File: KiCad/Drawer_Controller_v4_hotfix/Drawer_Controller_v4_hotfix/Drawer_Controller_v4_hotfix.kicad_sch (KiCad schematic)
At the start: 21 parts, among them J1 Conn_02x05_Odd_Even, J2 Conn_02x03_Odd_Even, J3 Conn_02x04_Odd_Even, U1 PESD2CANFD24L-TR, X1 RJ45_45_degree_angled, X2 Conn_01x02_2.5mm_JST_S02B-XAS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, X3 Conn_01x08_2.5mm_JST_S04B-XAS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, X4 Conn_02x03_3.0mm_Molex_Micro_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, X5 Conn_01x03_2.5mm_JST_S04B-XAS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, X6 Conn_01x04_2.5mm_JST_S04B-XAS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

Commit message: fix: adds `in_bom` attribute for two parts
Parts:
- X1, X4: now in the parts list
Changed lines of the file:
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@@
 		(unit 1)
 		(exclude_from_sim no)
-		(in_bom no)
+		(in_bom yes)
 		(on_board yes)
 		(dnp no)
@@
 		(unit 1)
 		(exclude_from_sim no)
-		(in_bom no)
-		(on_board yes)
-		(dnp no)
+		(in_bom yes)
+		(on_board yes)
+		(dnp no)

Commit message: feat: adds `durability` attribute to `Drawer_Controller_v4_hotfix`
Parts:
- C1: durability (none) -> 5000h@105°C
- X1: durability (none) -> 500 Mating cycles
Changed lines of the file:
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@@
 			)
 		)
+		(property "durability" ""
+			(at 340.36 80.01 0)
+			(effects
+				(font
+					(size 1.27 1.27)
+				)
+				(hide yes)
+			)
+		)
 		(pin "3"
 		)
@@
 			)
 		)
+		(property "durability" ""
+			(at 255.27 133.35 0)
+			(effects
+				(font
+					(size 1.27 1.27)
+				)
+				(hide yes)
+			)
+		)
 		(instances
 			(project "Drawer_Controller_v4"
@@
 			)
 		)
+		(property "durability" ""
+			(at 287.02 34.29 0)
+			(effects
+				(font
+					(size 1.27 1.27)
+				)
+				(hide yes)
+			)
+		)
 		(pin "6"
 		)
@@
 			)
 		)
+		(property "durability" ""
+			(at 97.79 121.92 0)
+			(effects
+				(font
+					(size 1.27 1.27)
+				)
+				(hide yes)
+			)
+		)
 		(pin "2"
 		)
@@
 			)
 		)
+		(property "durability" ""
+			(at 255.27 138.43 0)
+			(effects
+				(font
+					(size 1.27 1.27)
+				)
+				(hide yes)
+			)
+		)
 		(instances
 			(project "Drawer_Controller_v4"
@@
 			)
 		)
+		(property "durability" ""
+			(at 270.51 63.5 0)
+			(effects
+				(font
+					(size 1.27 1.27)
+				)
+				(hide yes)
+			)
+		)
 		(pin "3"
 		)
@@
 			)
 		)
+		(property "durability" ""
+			(at 280.67 138.43 0)
+			(effects
+				(font
+					(size 1.27 1.27)
+				)
+				(hide yes)
+			)
+		)
 		(instances
 			(project "Drawer_Controller_v4"
@@
 			)
 		)
+		(property "durability" "5000h@105°C"
+			(at 271.78 100.33 0)
+			(effects
+				(font
+					(size 1.27 1.27)
+				)
+				(hide yes)
+			)
+		)
 		(pin "2"
 		)
@@
 			)
 		)
+		(property "durability" ""
+			(at 218.44 45.72 0)
+			(effects
+				(font
+					(size 1.27 1.27)
+				)
+				(hide yes)
+			)
+		)
 		(pin "1"
 		)
@@
 			)
 		)
+		(property "durability" ""
+			(at 31.75 86.36 0)
+			(effects
+				(font
+					(size 1.27 1.27)
+				)
+				(hide yes)
+			)
+		)
 		(pin "2"
 		)
@@
 			)
 		)
+		(property "durability" ""
+			(at 255.27 143.51 0)
+			(effects
+				(font
+					(size 1.27 1.27)
+				)
+				(hide yes)
+			)
+		)
 		(instances
 			(project "Drawer_Controller_v4"
@@
 			)
 		)
+		(property "durability" "500 Mating cycles"
+			(at 30.48 45.72 0)
+			(effects
+				(font
+					(size 1.27 1.27)
+				)
+				(hide yes)
+			)
+		)
 		(pin "7"
 		)
@@
 			)
 		)
+		(property "durability" ""
+			(at 101.6 45.72 0)
+			(effects
+				(font
+					(size 1.27 1.27)
+				)
+				(hide yes)
+			)
+		)
 		(pin "3"
 		)
@@
 			)
 		)
+		(property "durability" ""
+			(at 337.82 36.83 0)
+			(effects
+				(font
+					(size 1.27 1.27)
+				)
+				(hide yes)
+			)
+		)
 		(pin "2"
 		)
@@
 			)
 		)
+		(property "durability" ""
+			(at 339.09 58.42 0)
+			(effects
+				(font
+					(size 1.27 1.27)
+				)
+				(hide yes)
+			)
+		)
 		(pin "1"
 		)
@@
 			)
 		)
+		(property "durability" ""
+			(at 274.32 106.68 0)
+			(effects
+				(font
+					(size 1.27 1.27)
+				)
+				(hide yes)
+			)
+		)
 		(pin "1"
 		)
@@
 			)
 		)
+		(property "durability" ""
+			(at 52.07 104.14 0)
+			(effects
+				(font
+					(size 1.27 1.27)
+				)
+				(hide yes)
+			)
+		)
 		(pin "2"
 		)
@@
 			)
 		)
+		(property "durability" ""
+			(at 45.72 80.01 0)
+			(effects
+				(font
+					(size 1.27 1.27)
+				)
+				(hide yes)
+			)
+		)
 		(pin "2"
 		)
@@
 			)
 		)
+		(property "durability" ""
+			(at 280.67 133.35 0)
+			(effects
+				(font
+					(size 1.27 1.27)
+				)
+				(hide yes)
+			)
+		)
 		(instances
 			(project "Drawer_Controller_v4"
@@
 			)
 		)
+		(property "durability" ""
+			(at 290.83 104.14 0)
+			(effects
+				(font
+					(size 1.27 1.27)
+				)
+				(hide yes)
+			)
+		)
 		(pin "3"
 		)
@@
 			(at 255.27 148.59 0)
 			(effects
+				(font
+					(size 1.27 1.27)
+				)
+				(hide yes)
+			)
+		)
+		(property "durability" ""
+			(at 255.27 148.59 0)
+			(effects

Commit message: feat: adds more `durability`attributes
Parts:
- X1: durability 500 Mating cycles -> 500 mating cycles
- X4: durability (none) -> 30 mating cycles
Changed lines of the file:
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@@
 			)
 		)
-		(property "durability" ""
+		(property "durability" "30 mating cycles"
 			(at 287.02 34.29 0)
 			(effects
@@
 			)
 		)
-		(property "durability" "500 Mating cycles"
+		(property "durability" "500 mating cycles"
 			(at 30.48 45.72 0)
 			(effects

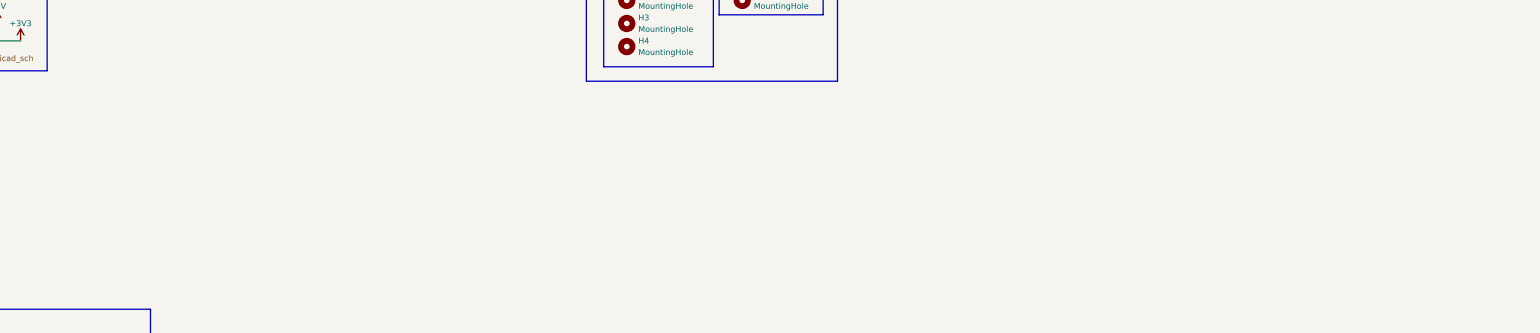
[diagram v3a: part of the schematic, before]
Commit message: docs: adds important hint for flashing the ESP's
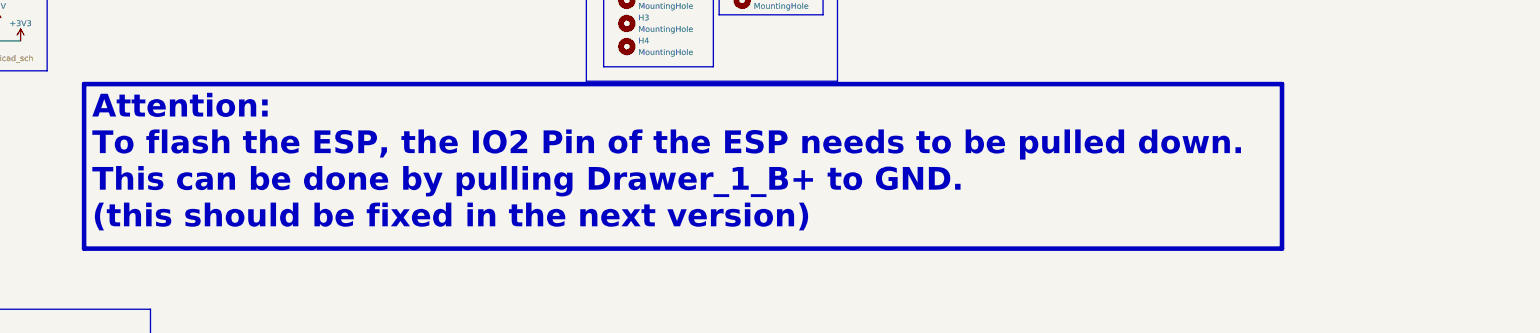
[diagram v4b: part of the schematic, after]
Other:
- note added: "Attention: To flash the ESP, the IO2 Pin of the ESP needs to be pulled down. This can be done by pulling Drawer_1_B+ to GND. (this should be fixed in the next version)"
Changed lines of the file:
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@@
+	)
+	(rectangle
+		(start 135.89 156.845)
+		(end 399.415 193.04)
+		(stroke
+			(width 1)
+			(type default)
+			(color 255 0 0 1)
+		)
+		(fill
+			(type none)
+		)
 	)
 	(rectangle
@@
 		)
 	)
+	(text "Attention:\nTo flash the ESP, the IO2 Pin of the ESP needs to be pulled down.\nThis can be done by pulling Drawer_1_B+ to GND.\n(this should be fixed in the next version)"
+		(exclude_from_sim no)
+		(at 137.668 173.99 0)
+		(effects
+			(font
+				(size 5 5)
+				(thickness 0.6)
+				(bold yes)
+				(color 255 0 0 1)
+			)
+			(justify left)
+		)
+	)
